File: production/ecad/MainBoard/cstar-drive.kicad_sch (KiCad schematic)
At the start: 53 parts, among them J1 B4B-PH-K-S, J2 B4B-PH-K-S, J3 Conn_01x03_Pin, J4 Conn_01x03_Pin, J5 Conn_01x03_Pin, J6 Conn_01x03_Pin, J7 Conn_01x03_Pin, J8 Conn_01x03_Pin, J9 Conn_01x03_Pin, U1 DRV8842PWPR, U2 DRV8842PWPR, X1 B2P-VH, X2 B2P-VH

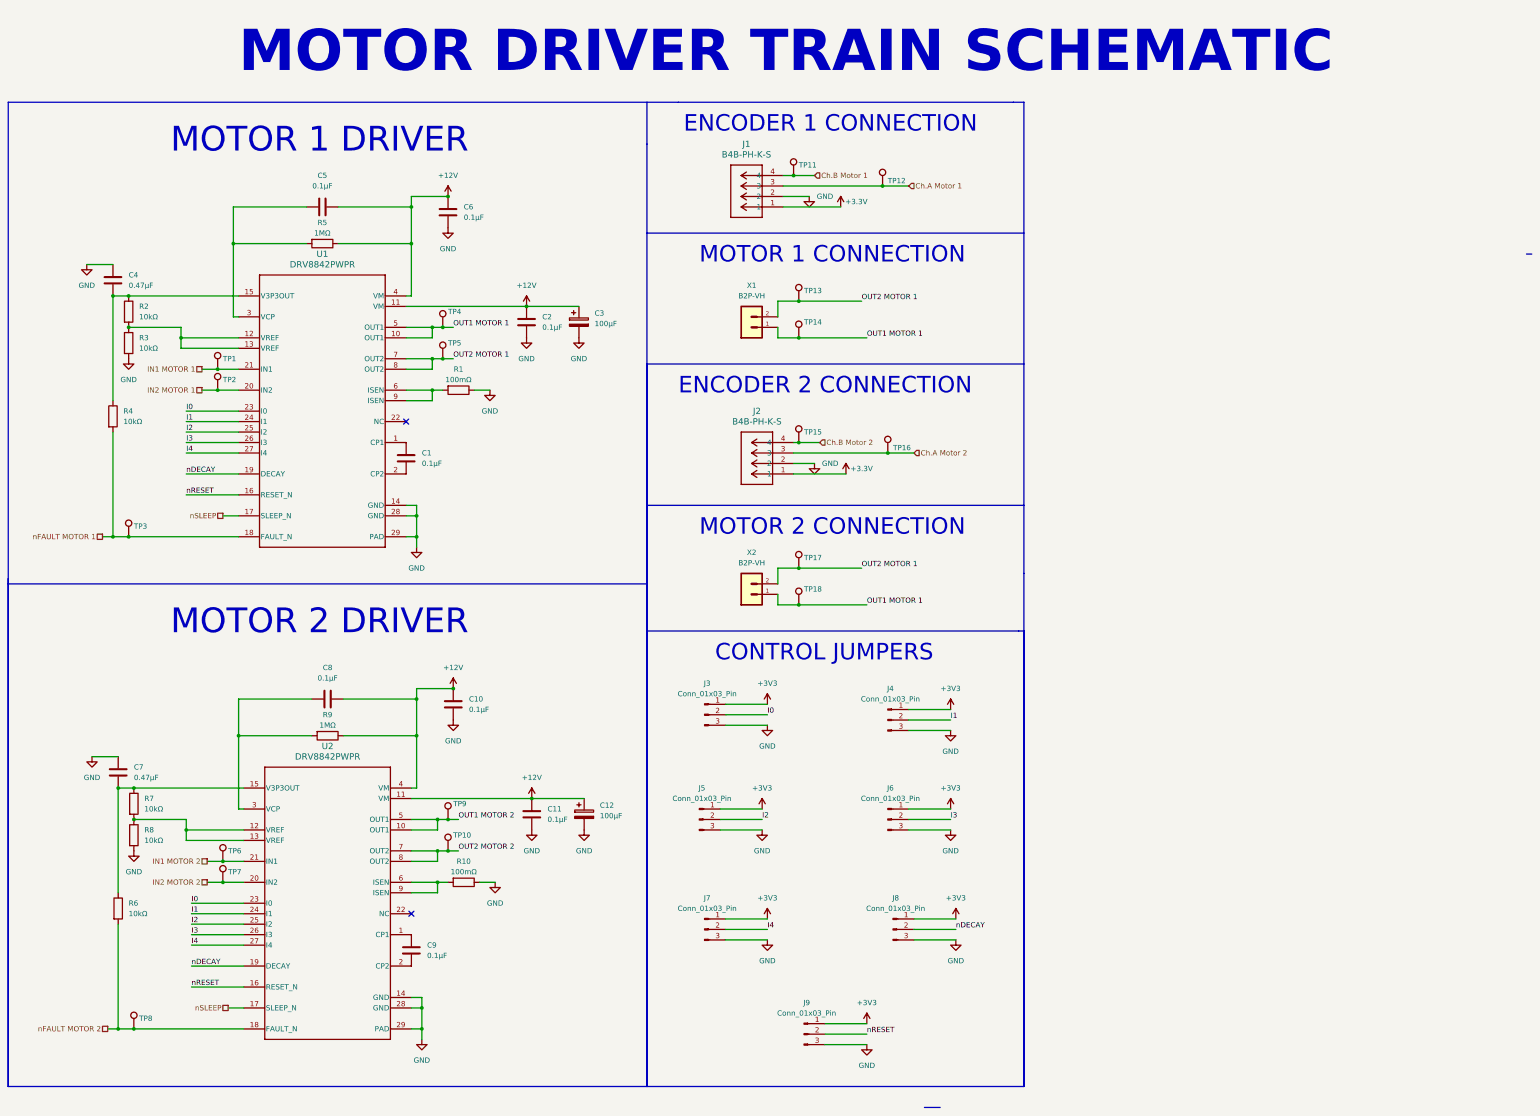
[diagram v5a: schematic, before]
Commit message: "Added Protective Diodes"
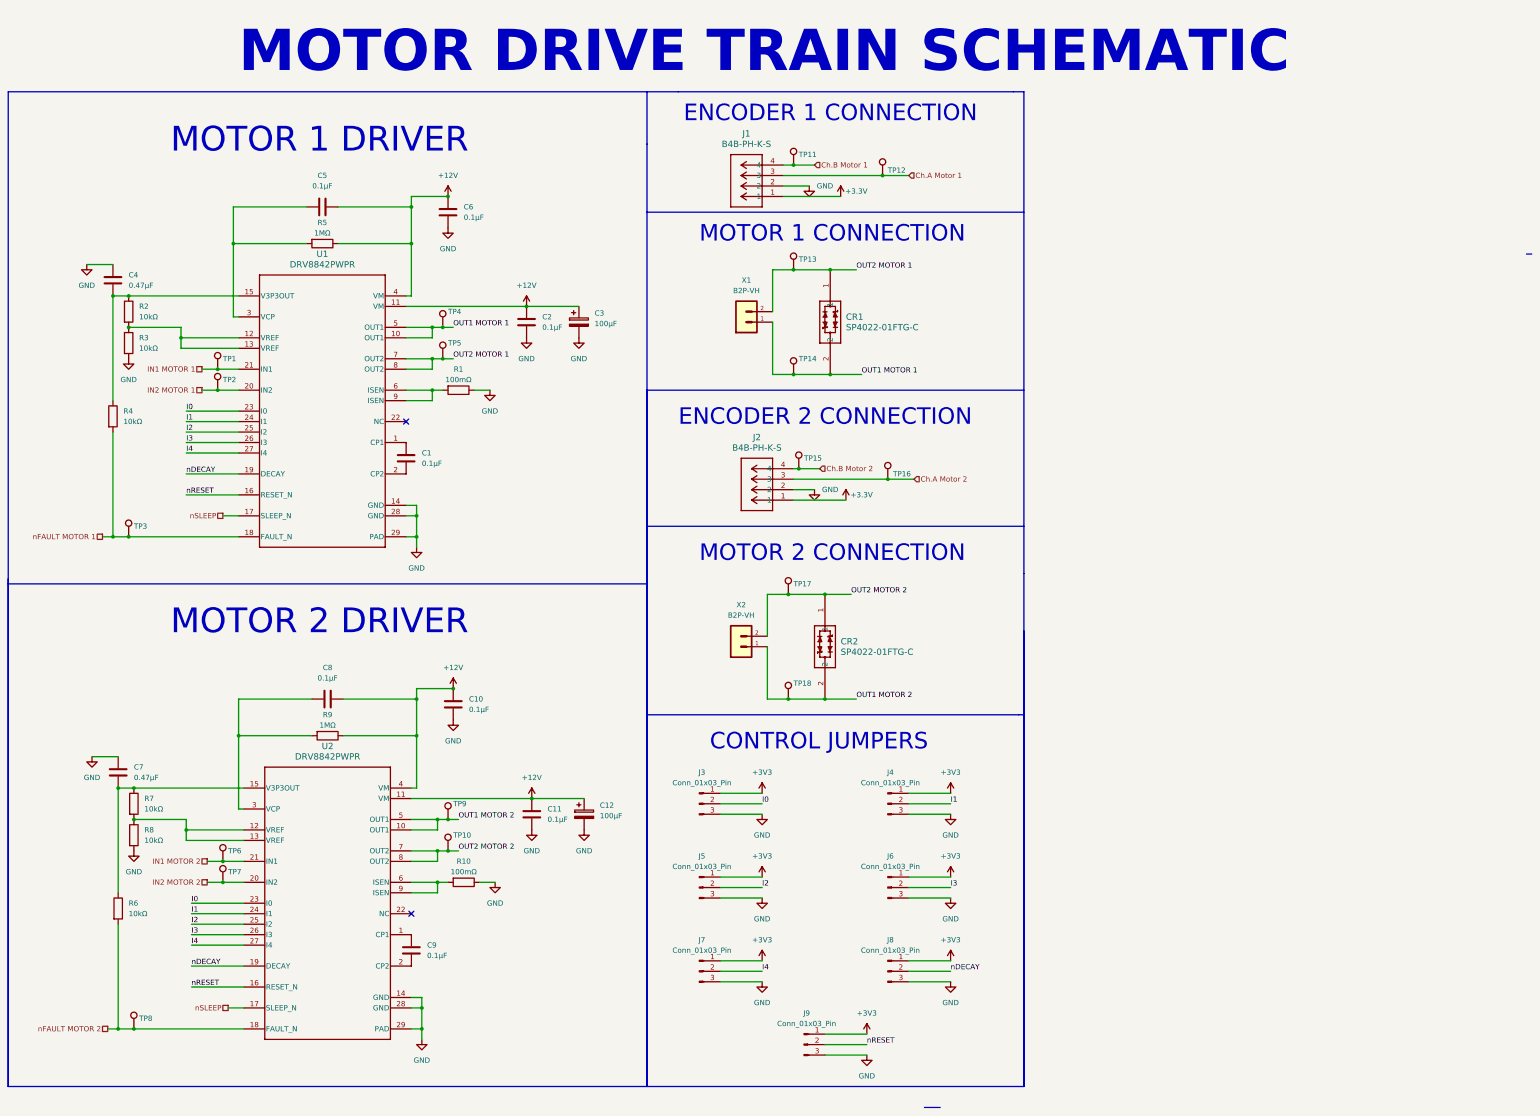
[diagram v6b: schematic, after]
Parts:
- added CR1, CR2: SP4022-01FTG-C, ZDO_SP4022_LTF, symbol SP4022_01FTG_C:SP4022-01FTG-C
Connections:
- net OUT1 MOTOR 1: now also CR1.2; no longer TP18.1, X2.1
- net OUT1 MOTOR 2: now also TP18.1, X2.1, CR2.2
- net OUT2 MOTOR 1: now also CR1.1; no longer TP17.1, X2.2
- net OUT2 MOTOR 2: now also TP17.1, X2.2, CR2.1
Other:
- note added: "MOTOR DRIVE TRAIN SCHEMATIC"
- note removed: "MOTOR DRIVER TRAIN SCHEMATIC"
- moved on the sheet: J1, J2, J3, J4, J5, J6, J7, J8, J9, TP11, TP12, TP13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

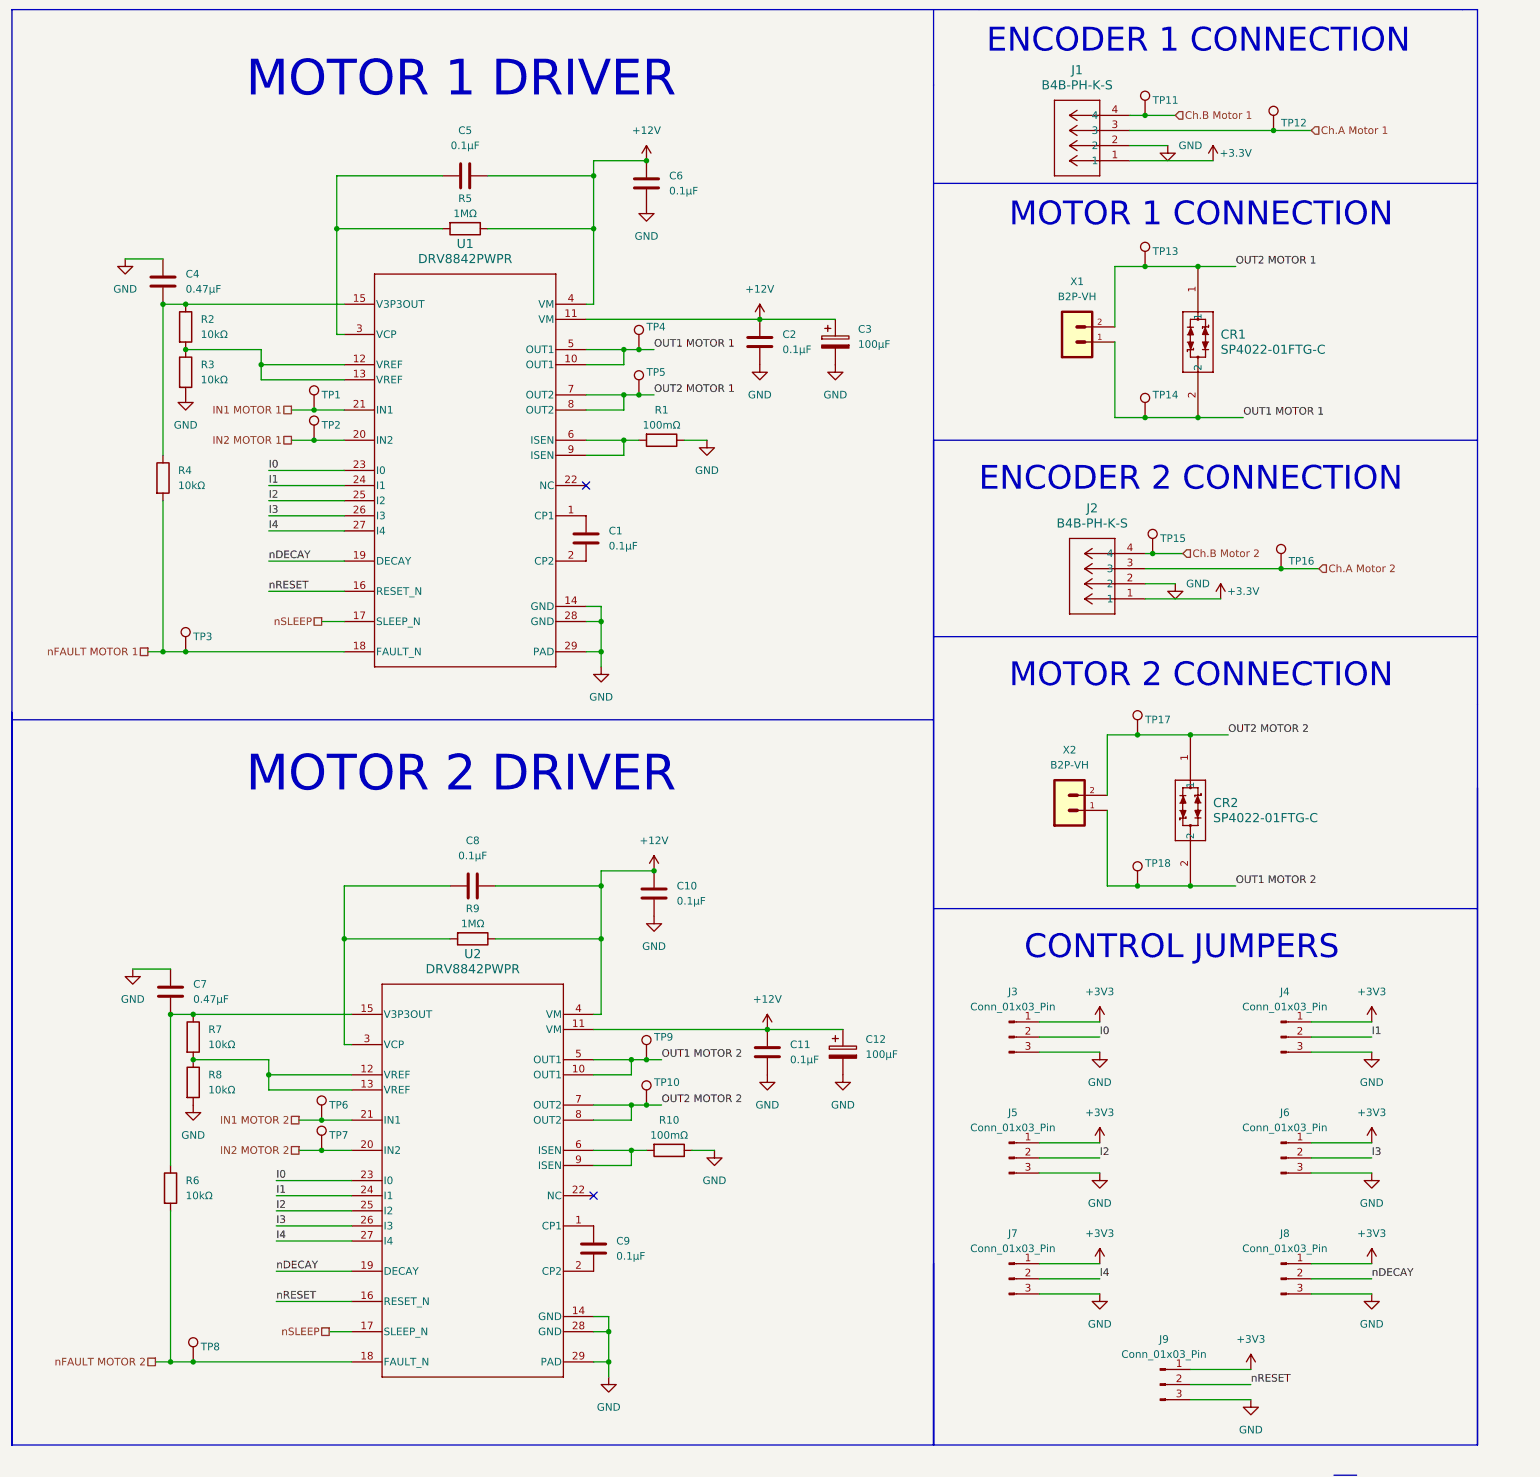
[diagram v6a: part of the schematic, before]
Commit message: "Added Global Labels"
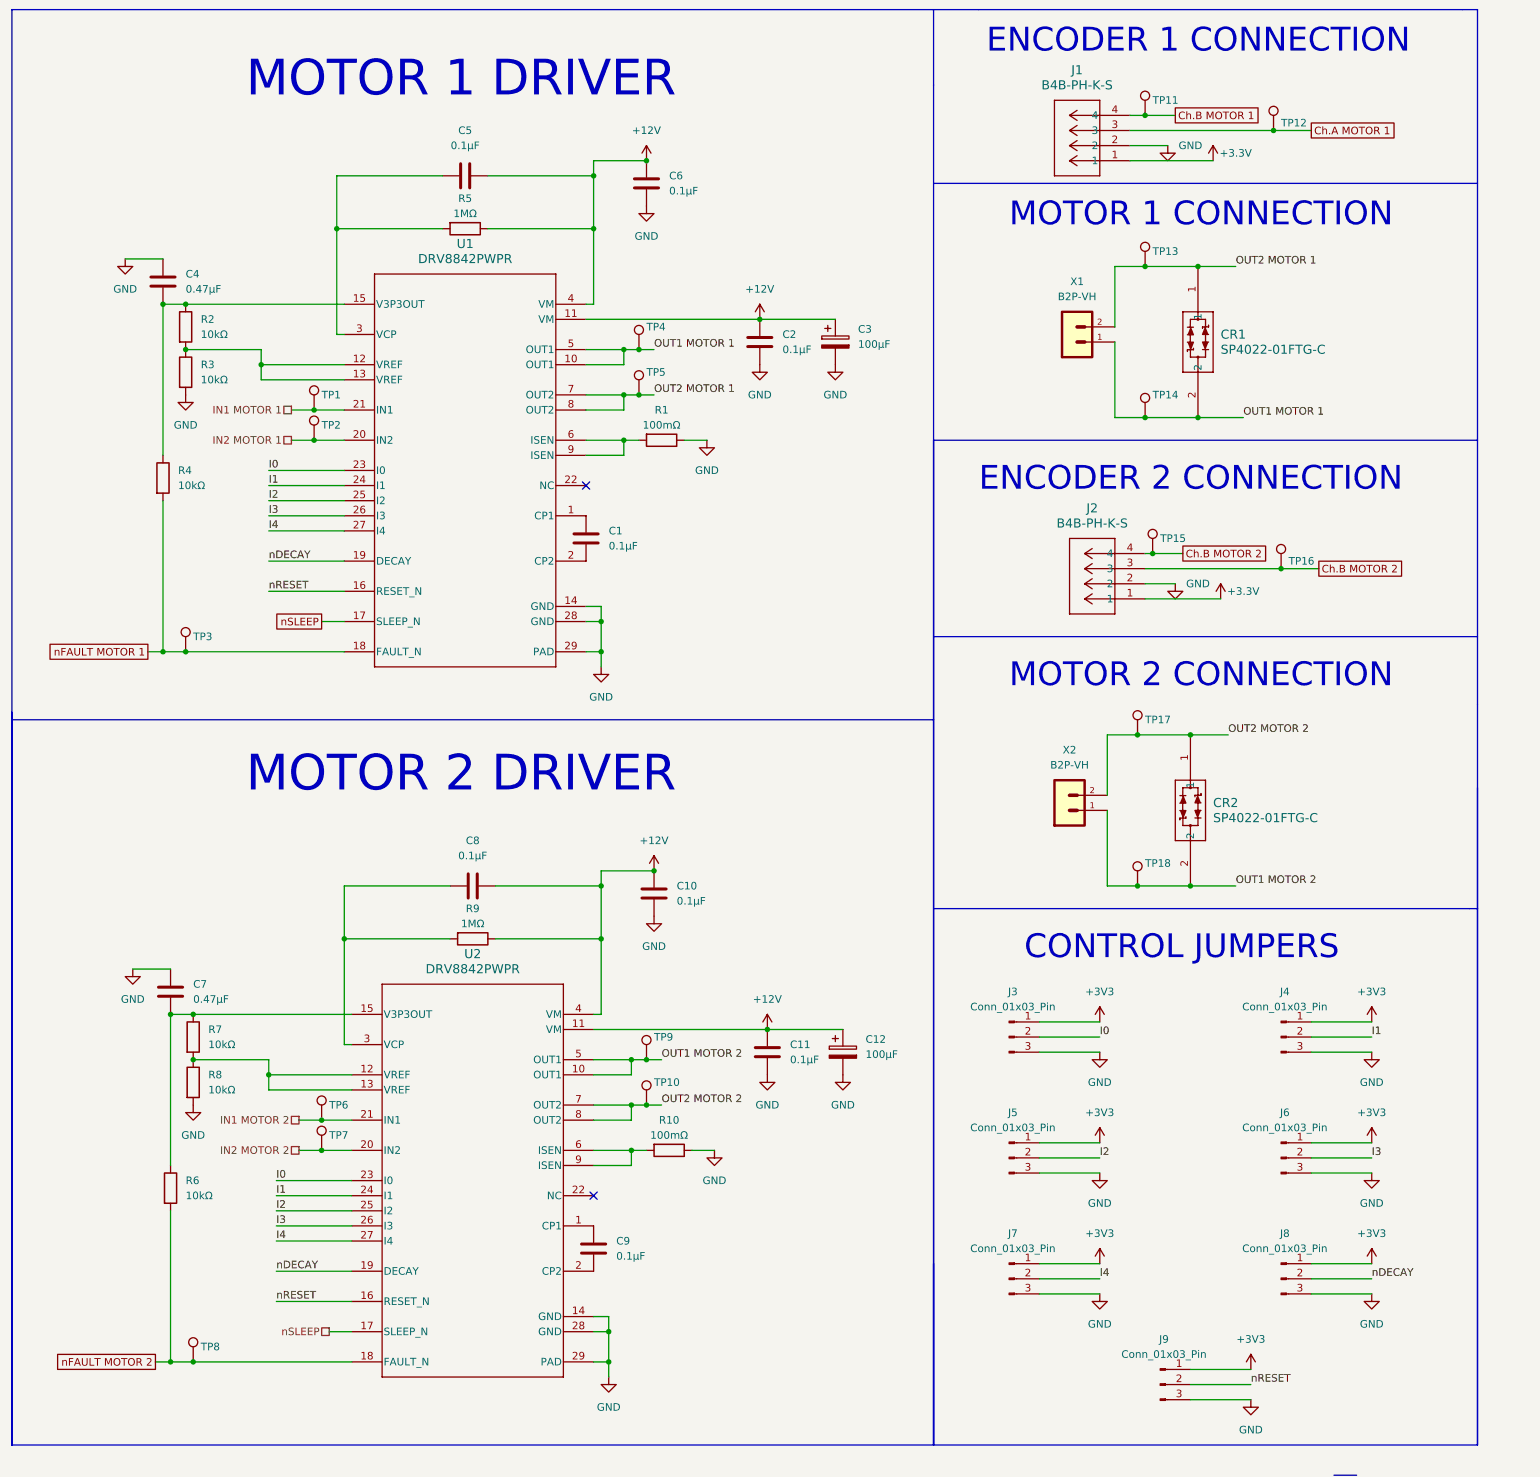
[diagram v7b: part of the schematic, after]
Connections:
- net Ch.B Motor 2 is gone; now on net Ch.B MOTOR 2: J2.4, TP15.1
- net Ch.A Motor 1 renamed Ch.A MOTOR 1
- net Ch.A Motor 2 renamed Ch.B MOTOR 2
- net Ch.B Motor 1 renamed Ch.B MOTOR 1
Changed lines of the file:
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@@
     (effects (font (size 1.27 1.27)) (justify left bottom))
   )
-  (hierarchical_label "nFAULT MOTOR 1" (shape passive) (at 58.42 144.78 180) (fields_autoplaced)
+  (global_label "Ch.B MOTOR 1" (shape passive) (at 231.14 54.61 0) (fields_autoplaced)
+    (effects (font (size 1.27 1.27)) (justify left))
+    (property "Intersheetrefs" "${INTERSHEET_REFS}" (at 246.8024 54.61 0)
+      (effects (font (size 1.27 1.27)) (justify left) hide)
+    )
+  )
+  (global_label "nFAULT MOTOR 1" (shape passive) (at 58.42 144.78 180) (fields_autoplaced)
     (effects (font (size 1.27 1.27)) (justify right))
+    (property "Intersheetrefs" "${INTERSHEET_REFS}" (at 40.399 144.78 0)
+      (effects (font (size 1.27 1.27)) (justify right) hide)
+    )
   )
-  (hierarchical_label "Ch.B Motor 1" (shape input) (at 231.14 54.61 0) (fields_autoplaced)
+  (global_label "nFAULT MOTOR 2" (shape passive) (at 59.69 264.16 180) (fields_autoplaced)
+    (effects (font (size 1.27 1.27)) (justify right))
+    (property "Intersheetrefs" "${INTERSHEET_REFS}" (at 41.669 264.16 0)
+      (effects (font (size 1.27 1.27)) (justify right) hide)
+    )
+  )
+  (global_label "Ch.A MOTOR 1" (shape passive) (at 254 57.15 0) (fields_autoplaced)
     (effects (font (size 1.27 1.27)) (justify left))
+    (property "Intersheetrefs" "${INTERSHEET_REFS}" (at 269.481 57.15 0)
+      (effects (font (size 1.27 1.27)) (justify left) hide)
+    )
+  )
+  (global_label "Ch.B MOTOR 2" (shape passive) (at 232.41 128.27 0) (fields_autoplaced)
+    (effects (font (size 1.27 1.27)) (justify left))
+    (property "Intersheetrefs" "${INTERSHEET_REFS}" (at 248.0724 128.27 0)
+      (effects (font (size 1.27 1.27)) (justify left) hide)
+    )
+  )
+  (global_label "Ch.B MOTOR 2" (shape passive) (at 255.27 130.81 0) (fields_autoplaced)
+    (effects (font (size 1.27 1.27)) (justify left))
+    (property "Intersheetrefs" "${INTERSHEET_REFS}" (at 270.9324 130.81 0)
+      (effects (font (size 1.27 1.27)) (justify left) hide)
+    )
+  )
+  (global_label "nSLEEP" (shape passive) (at 87.63 139.7 180) (fields_autoplaced)
+    (effects (font (size 1.27 1.27)) (justify right))
+    (property "Intersheetrefs" "${INTERSHEET_REFS}" (at 78.8015 139.7 0)
+      (effects (font (size 1.27 1.27)) (justify right) hide)
+    )
   )
   (hierarchical_label "IN1 MOTOR 2" (shape passive) (at 83.82 223.52 180) (fields_autoplaced)
@@
     (effects (font (size 1.27 1.27)) (justify right))
   )
-  (hierarchical_label "Ch.B Motor 2" (shape input) (at 232.41 128.27 0) (fields_autoplaced)
-    (effects (font (size 1.27 1.27)) (justify left))
-  )
   (hierarchical_label "IN1 MOTOR 1" (shape passive) (at 82.55 104.14 180) (fields_autoplaced)
-    (effects (font (size 1.27 1.27)) (justify right))
-  )
-  (hierarchical_label "nSLEEP" (shape passive) (at 87.63 139.7 180) (fields_autoplaced)
-    (effects (font (size 1.27 1.27)) (justify right))
-  )
-  (hierarchical_label "nFAULT MOTOR 2" (shape passive) (at 59.69 264.16 180) (fields_autoplaced)
     (effects (font (size 1.27 1.27)) (justify right))
   )
@@
     (effects (font (size 1.27 1.27)) (justify right))
   )
-  (hierarchical_label "Ch.A Motor 2" (shape input) (at 255.27 130.81 0) (fields_autoplaced)
-    (effects (font (size 1.27 1.27)) (justify left))
-  )
-  (hierarchical_label "Ch.A Motor 1" (shape input) (at 254 57.15 0) (fields_autoplaced)
-    (effects (font (size 1.27 1.27)) (justify left))
-  )
   (symbol (lib_id "power:+12V") (at 161.29 88.9 0) (unit 1)
